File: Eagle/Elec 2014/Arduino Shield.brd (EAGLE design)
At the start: 102 x 53.3 mm, 63 parts, among them Q1 BC857B, Q2 BC857B, U1 TLC555, U2 SN74HC14PW

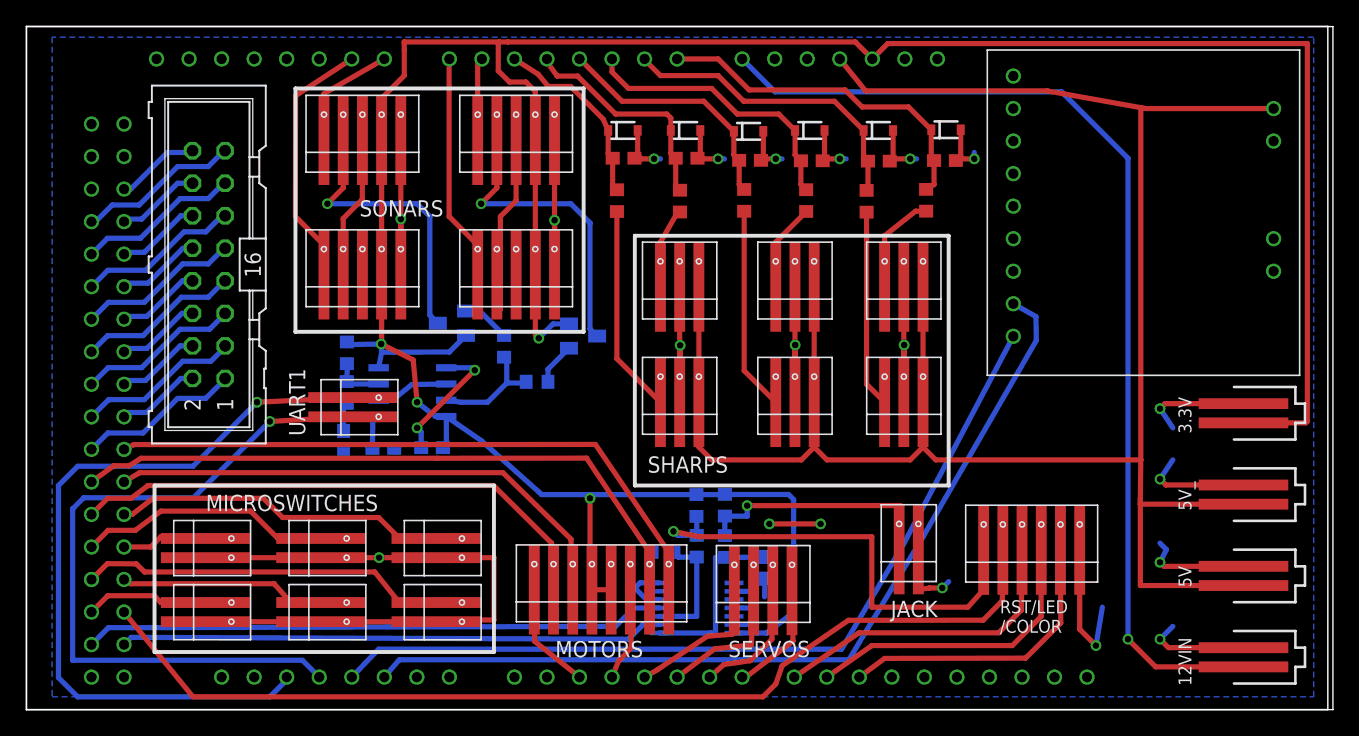
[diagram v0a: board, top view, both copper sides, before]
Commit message: New servo & aux motor board, updated Arduino shield, new battery board 2014
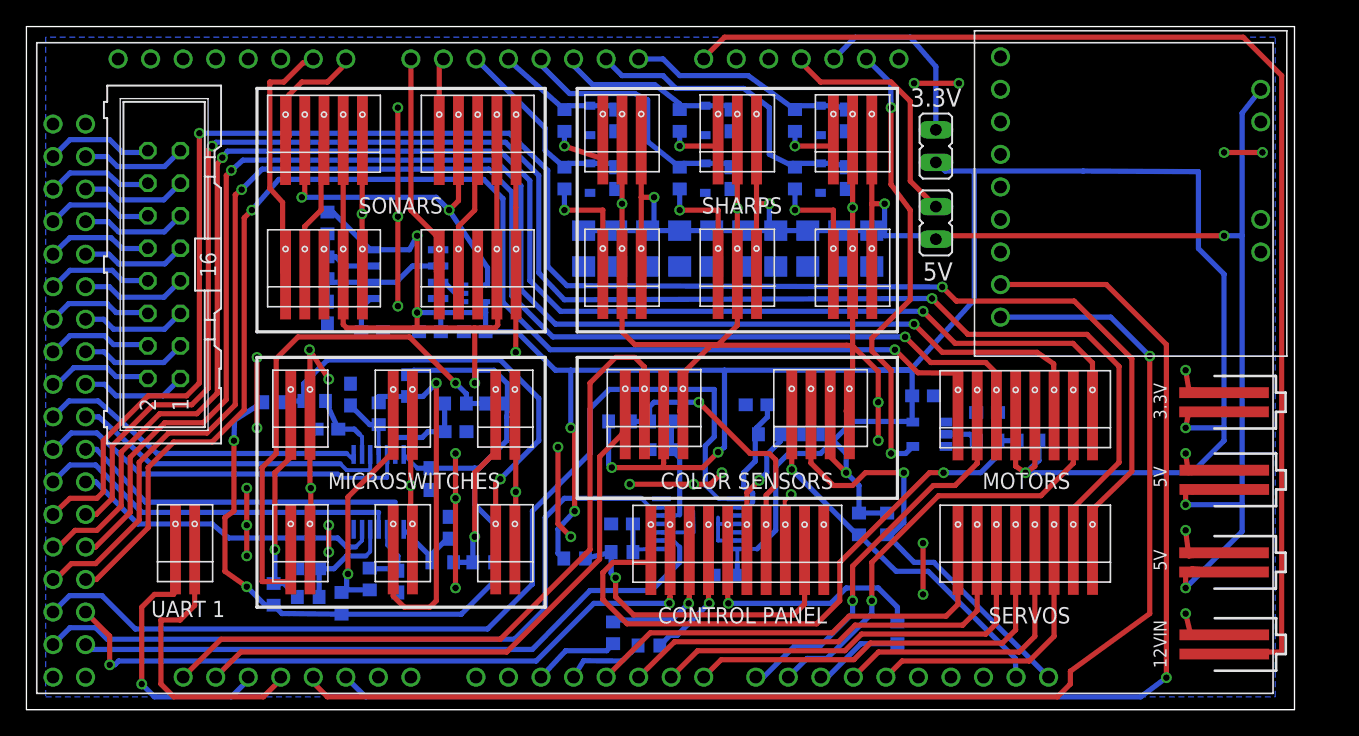
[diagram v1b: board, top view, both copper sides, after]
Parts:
- removed 5V_: 87438-02, con-molex:87438-02
- removed JACK: 87437-0243, custom:87437-0243
- removed Q1, Q2: BC857B, transistor-pnp:SOT23
- removed RST/LED/COLOR: 87437-0643, custom:87437-0643
- added 5V1: 87438-02, con-molex:87438-02
- added C12, C13, C18, C20, C21, C22, C23, C24: 10uF, rcl:C0603
- added C14, C25, C26, C27, C28, C29, C30, C31, C32, C33: 47uF, rcl:C1206
- added C15, C16, C17, C19: 0.1uF, rcl:C0603
- added CONTROL: 87437-1043, custom:87437-1043
- added IC1: 74LVC1G17DBV, 74xx-little-de:SOT23-5
- added IC2: 74LVC1G04DCK, 74xx-little-us:SC70-5
- added JP1, JP2: (no value), jumper:JP1
- added R13: 330, rcl:R0603
- added R14: 68, rcl:R0603
- added R15: 33, rcl:R0603
- added R16, R18, R21, R23, R25, R27, R29: 1K, rcl:R0603
- added R17, R19, R20, R22, R24, R26, R28: 10K, rcl:R0603
- added R30, R31: 1.5K, rcl:R0603
- added RBG_SENSOR2, RGB_SENSOR1: 87437-0443, custom:87437-0443
- added U3: SN74HC14PW, custom:SOP65P640X120-14N
- C1, C4, C5, C6, C7, C9: value 0.1uF -> 1uF
- C2: value 0.1uF -> 0.01uF
- R1, R2, R3, R4, R5, R6: value 10K -> 470
- R12: value 10K -> 1K
- SERVOS: value 87437-0443 -> 87437-0843; device custom:87437-0443 -> custom:87437-0843
- moved MOTORS 35.8 mm to (78.0, 23.0)
- moved C11 27.6 mm to (75.0, 23.2), turned to 180 degrees
- moved R10 26.4 mm to (78.2, 21.0), turned to 180 degrees
- moved R9 24.1 mm to (75.0, 21.0), turned to 180 degrees
- moved SERVOS 20.7 mm to (78.0, 12.5)
- moved UART1 17.0 mm to (12.5, 12.5), turned to 90 degrees
- moved USW4 12.9 mm to (21.5, 23.0), turned to 90 degrees
- moved R7 12.4 mm to (42.8, 11.8), turned to 0 degrees
- moved SHARP3 12.3 mm to (55.5, 44.5)
- moved SHARP5 12.3 mm to (46.5, 44.5)
- moved USW5 12.3 mm to (29.5, 23.0), turned to 90 degrees
- moved SHARP1 12.2 mm to (64.5, 44.5)
- moved R6 12.0 mm to (60.0, 46.0), flipped to the bottom
- moved USW6 11.9 mm to (37.5, 23.0), turned to 90 degrees
- moved R4 11.7 mm to (51.0, 46.0), flipped to the bottom
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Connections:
- net N$10 renamed RX1
- net N$11 renamed JACK
- net N$9 renamed TX1
- removed net N$37: Q2.1, R12.1
- removed net N$38: Q1.1, R11.1
- removed net N$46: Q2.3, SONAR_BL.P$2
- new net BLUE: R15.1, U$1.PWM10
- new net BTN1: U$1.23, U2.6
- new net BTN2: U$1.25, U2.8
- new net BUT1: CONTROL.P$7, R16.2, R17.1
- new net BUT2: CONTROL.P$6, R18.2, R19.1
- new net GREEN: R14.1, U$1.PWM3
- new net N$1: JP1.1, U$1.3.3V
- new net N$10: C18.2, R12.1, U3.13
- new net N$11: C13.1, R18.1, U2.9
- new net N$15: CONTROL.P$5, R15.2
- new net N$16: CONTROL.P$4, R14.2
- new net N$17: CONTROL.P$3, R13.2
- new net N$18: SERVOS.P$8, U$1.31
- new net N$19: R20.1, R21.2, USW2.P$1
- new net N$20: C20.2, R21.1, U3.11
- new net N$21: R22.1, R23.2, USW3.P$1
- new net N$22: C21.2, R23.1, U3.9
- new net N$23: R24.1, R25.2, USW4.P$1
- new net N$24: C22.2, R25.1, U3.5
- new net N$25: R26.1, R27.2, USW5.P$1
- new net N$26: C23.2, R27.1, U3.3
- new net N$28: R28.1, R29.2, USW6.P$1
- new net N$29: C24.2, R29.1, U3.1
- new net N$7: IC1.4, U$1.RESET
- new net N$8: JP2.1, U$1.5V3
- new net N$9: R11.1, R12.2, USW1.P$1
- new net RED: R13.1, U$1.PWM2
- new net SCL: RGB_SENSOR1.P$2, U$1.SCL
- new net SCL1: R31.1, RBG_SENSOR2.P$2, U$1.SCL1
- new net SDA: RGB_SENSOR1.P$1, U$1.SDA
- new net SDA1: R30.1, RBG_SENSOR2.P$1, U$1.SDA1
- net 3.3VCC: now also C15.1, C16.2, C17.2, C19.1, IC1.5, IC2.5, JP1.2, R11.2, R17.2, R19.2, R20.2, R22.2, R24.2, R26.2, R28.2, R30.2, R31.2, RBG_SENSOR2.P$3, RGB_SENSOR1.P$3, U3.14; no longer Q1.2, Q2.2, U$1.3.3V
- net 5VCC: now also 5V1.1, C14.2, C25.2, C26.2, C27.2, C28.2, C29.2, C30.2, C31.2, C32.2, C33.2, JP2.2; no longer 5V_.1, U$1.5V3
- net COLOR: now also CONTROL.P$2; no longer RST/LED/COLOR.P$2
- net GND: now also 5V1.2, C12.2, C13.2, C14.1, C15.2, C16.1, C17.1, C18.1, C19.2, C20.1, C21.1, C22.1, C23.1, C24.1, C25.1, C26.1, C27.1, C28.1, C29.1, C30.1, C31.1, C32.1, C33.1, CONTROL.P$8, IC1.3, IC2.3, RBG_SENSOR2.P$4, RGB_SENSOR1.P$4, U$1.GND, U$1.GND2, U$1.GND3, U$1.GND5, U2.3, U3.7; no longer 5V_.2, JACK.P$2, RST/LED/COLOR.P$6, U2.5, U2.9
- net MOTOR1_BREAK: now also U$1.27; no longer U$1.32
- net MOTOR1_DIR: now also U$1.PWM8; no longer U$1.31
- net MOTOR1_PWM: now also U$1.26; no longer U$1.PWM2
- net MOTOR2_BREAK: now also U$1.29; no longer U$1.34
- net MOTOR2_DIR: now also U$1.PWM9; no longer U$1.33
- net MOTOR2_PWM: now also U$1.28; no longer U$1.PWM3
- net N$12: now also SERVOS.P$5, U$1.PWM11; no longer RST/LED/COLOR.P$4, U$1.PWM9
- net N$13: now also SERVOS.P$6, U$1.PWM12; no longer RST/LED/COLOR.P$5, U$1.PWM10
- net N$14: now also SERVOS.P$7, U$1.30; no longer U$1.23, U2.4
- net N$2: now also C12.1, R16.1, U2.5; no longer RST/LED/COLOR.P$3, U$1.PWM8
- net N$27: now also CONTROL.P$9; no longer JACK.P$1
- net N$36: now also IC2.2; no longer R11.2, R12.2
- net N$44: now also U$1.38; no longer U$1.35
- net N$45: now also IC2.4, SONAR_BL.P$2; no longer Q1.3
- net N$47: now also U$1.39; no longer U$1.36
- net N$48: now also U$1.40; no longer U$1.37
- net N$49: now also U$1.41; no longer U$1.38
- net N$50: now also U$1.42; no longer U$1.39
- net N$51: now also U$1.43; no longer U$1.40
- net N$52: now also U$1.44; no longer U$1.41
- net N$53: now also U$1.45; no longer U$1.42
- net N$54: now also U$1.46; no longer U$1.43
- net N$55: now also U$1.47; no longer U$1.44
- net N$56: now also U$1.48; no longer U$1.45
- net N$57: now also U$1.49; no longer U$1.46
- net N$58: now also U$1.50; no longer U$1.47
- net N$59: now also U$1.51; no longer U$1.48
- net N$60: now also U$1.52; no longer U$1.49
- net N$61: now also U$1.53; no longer U$1.50
- net N$71: now also IC1.2; no longer U2.3
- net RST: now also CONTROL.P$1; no longer RST/LED/COLOR.P$1
- net USW1: now also U$1.34, U3.2; no longer U$1.25, USW1.P$1
- net USW2: now also U$1.33, U3.4; no longer U$1.26, USW2.P$1
- net USW3: now also U$1.32, U3.6; no longer U$1.27, USW3.P$1
- net USW4: now also U$1.37, U3.8; no longer U$1.28, USW4.P$1
- net USW5: now also U$1.36, U3.10; no longer U$1.29, USW5.P$1
- net USW6: now also U$1.35, U3.12; no longer U$1.30, USW6.P$1
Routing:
- net N$18: track 0.00 -> 138.2 mm, vias 0 -> 2
- net 3.3VCC: track 234.5 -> 356.8 mm, vias 4 -> 12
- net MOTOR2_PWM: track 7.32 -> 116.1 mm, vias 0 -> 2
- net MOTOR1_PWM: track 8.51 -> 107.0 mm, vias 0 -> 2
- net N$14: track 45.5 -> 133.6 mm, vias 0 -> 2
- net BTN2: track 0.00 -> 77.0 mm
- net MOTOR1_BREAK: track 41.2 -> 113.8 mm, vias 0 -> 2
- net MOTOR2_BREAK: track 50.0 -> 122.5 mm, vias 0 -> 2
- net SCL: track 0.00 -> 58.0 mm
- net BTN1: track 0.00 -> 57.4 mm
- net SDA: track 0.00 -> 45.8 mm
- net N$9: track 0.00 -> 42.1 mm, vias 0 -> 1
- net RX1: track 59.9 -> 22.0 mm
- net N$21: track 0.00 -> 36.4 mm, vias 0 -> 1
- net UM6_RX: track 69.7 -> 106.1 mm, vias 0 -> 1
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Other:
- board size 102 x 53.3 mm -> 99 x 53.3 mm
- board text added: "3.3V"
- board text added: "5V"
- board text added: "COLOR SENSORS"
- board text added: "CONTROL PANEL"
- board text added: "UART 1"
- board text removed: "RST/LED /COLOR"

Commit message: Small fixes after testing cards
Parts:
- C2: value 0.01uF -> 0.1uF
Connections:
- net MOTOR1_BREAK: now also MOTORS.P$6, U$1.28; no longer MOTORS.P$3, U$1.27
- net MOTOR1_DIR: now also MOTORS.P$7, U$1.PWM9; no longer MOTORS.P$2, U$1.PWM8
- net MOTOR1_PWM: now also MOTORS.P$8, U$1.29; no longer MOTORS.P$1, U$1.26
- net MOTOR2_BREAK: now also MOTORS.P$1, U$1.26; no longer MOTORS.P$8, U$1.29
- net MOTOR2_DIR: now also MOTORS.P$2, U$1.PWM8; no longer MOTORS.P$7, U$1.PWM9
- net MOTOR2_PWM: now also MOTORS.P$3, U$1.27; no longer MOTORS.P$6, U$1.28
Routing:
- net MOTOR2_BREAK: track 122.5 -> 107.0 mm
- net MOTOR1_PWM: track 107.0 -> 122.5 mm
- net MOTOR2_DIR: track 35.2 -> 30.1 mm
- net MOTOR1_DIR: track 30.1 -> 35.2 mm
- net MOTOR2_PWM: track 116.1 -> 113.8 mm
- net MOTOR1_BREAK: track 113.8 -> 116.1 mm
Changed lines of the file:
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@@
 <attribute name="OC_FARNELL" value="9488227" x="7.91" y="-28.23" size="1.778" layer="28" rot="MR0" display="off"/>
 </element>
-<element name="C2" library="rcl" package="C0603" value="0.01uF" x="27" y="29.5" smashed="yes" rot="MR180"/>
+<element name="C2" library="rcl" package="C0603" value="0.1uF" x="27" y="29.5" smashed="yes" rot="MR180"/>
 <element name="RA" library="rcl" package="R0603" value="330K" x="23.5" y="38" smashed="yes" rot="MR90"/>
 <element name="RB" library="rcl" package="R0603" value="3.3K" x="23.5" y="34.5" smashed="yes" rot="MR90"/>
@@
 <wire x1="77.23" y1="6.23" x2="77.23" y2="12.46" width="0.4064" layer="1"/>
 </signal>
-<signal name="MOTOR2_DIR">
+<signal name="MOTOR1_DIR">
 <contactref element="U$1" pad="PWM9"/>
 <contactref element="MOTORS" pad="P$7"/>
@@
 <via x="66" y="8.5" extent="1-16" drill="0.5"/>
 </signal>
-<signal name="MOTOR1_DIR">
+<signal name="MOTOR2_DIR">
 <contactref element="U$1" pad="PWM8"/>
 <contactref element="MOTORS" pad="P$2"/>
@@
 <wire x1="40.5" y1="43.65" x2="42" y2="42.35" width="0.4064" layer="16"/>
 </signal>
-<signal name="MOTOR1_PWM">
+<signal name="MOTOR2_BREAK">
 <contactref element="MOTORS" pad="P$1"/>
 <contactref element="U$1" pad="26"/>
@@
 <wire x1="14.5" y1="20.9" x2="17" y2="23.4" width="0.4064" layer="1"/>
 </signal>
-<signal name="MOTOR1_BREAK">
+<signal name="MOTOR2_PWM">
 <contactref element="MOTORS" pad="P$3"/>
 <contactref element="U$1" pad="27"/>
@@
 <wire x1="14.1" y1="21.6" x2="16.3" y2="23.8" width="0.4064" layer="1"/>
 </signal>
-<signal name="MOTOR2_PWM">
+<signal name="MOTOR1_BREAK">
 <contactref element="MOTORS" pad="P$6"/>
 <contactref element="U$1" pad="28"/>
@@
 <wire x1="13.8" y1="22.4" x2="15.6" y2="24.2" width="0.4064" layer="1"/>
 </signal>
-<signal name="MOTOR2_BREAK">
+<signal name="MOTOR1_PWM">
 <contactref element="MOTORS" pad="P$8"/>
 <contactref element="U$1" pad="29"/>
